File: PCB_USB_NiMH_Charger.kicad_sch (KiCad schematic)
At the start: 45 parts, among them J1 USB_C_Receptacle_Simple, J2 Conn_02x01, J3 Conn_02x01, J4 Conn_02x01, Q1 2SA1015, Q2 2SC1815, Q3 2SB834, Q4 2SC1815, Q5 2SB834, U1 LM393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

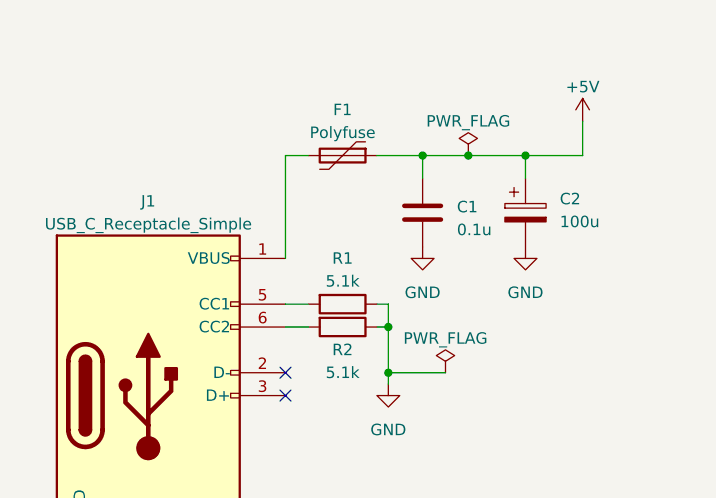
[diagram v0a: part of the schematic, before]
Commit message: 初版の知見を反映した細かい調整
* VBUSをラベル付け。
* USBコネクタのパッドの穴のサイズを0.9mmに縮小。
* ネットクラスに "Power" を追加。
* D1用にDO-41Sのフットプリントを追加。
* R8, R9, R14, R15 の配置を調整。
* 配線を調整。
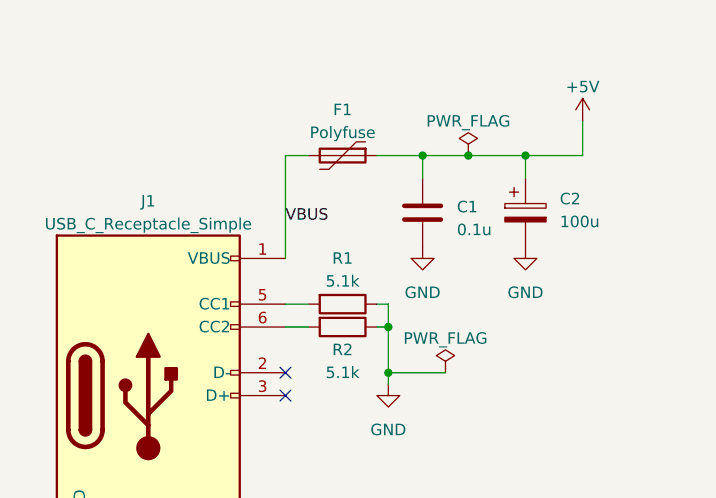
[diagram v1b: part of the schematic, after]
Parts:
- D1: footprint Diode_THT:D_DO-41_SOD81_P7.62mm_Horizontal -> mylib:D_DO-41S_SOD81_P7.62mm_Horizontal
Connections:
- net VBUS: now reaches F1.2, J1.1 (VBUS), J1.A9 (VBUS), J1.B4 (VBUS), J1.B9 (VBUS)
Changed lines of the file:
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@@
+    (effects (font (size 1.27 1.27)) (justify left bottom))
+  )
+  (label "VBUS" (at 48.26 38.1 0) (fields_autoplaced)
     (effects (font (size 1.27 1.27)) (justify left bottom))
   )
@@
       (effects (font (size 1.27 1.27)))
     )
-    (property "Footprint" "Diode_THT:D_DO-41_SOD81_P7.62mm_Horizontal" (at 94.615 132.08 0)
-      (effects (font (size 1.27 1.27)) hide)
-    )
+    (property "Footprint" "mylib:D_DO-41S_SOD81_P7.62mm_Horizontal" (at 94.615 132.08 0)
+      (effects (font (size 1.27 1.27)) hide)
+    )

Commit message: Update title to rev. 2
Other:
- title: USB NiMH slow charger -> USB NiMH slow charger rev. 2
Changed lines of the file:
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@@
   (paper "A4")
   (title_block
-    (title "USB NiMH slow charger")
-    (date "2023-03-05")
+    (title "USB NiMH slow charger rev. 2")
+    (date "2023-03-22")
     (company "K.Takata")
   )

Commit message: Update revision
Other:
- title: USB NiMH slow charger rev. 2 -> USB NiMH slow charger
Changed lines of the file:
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@@
   (paper "A4")
   (title_block
-    (title "USB NiMH slow charger rev. 2")
+    (title "USB NiMH slow charger")
     (date "2023-03-22")
+    (rev "2")
     (company "K.Takata")
   )
